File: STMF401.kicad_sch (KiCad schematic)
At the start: 13 parts, among them Y1 X322525MQB4SI

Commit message: feat: firs complete version schemattic
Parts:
- added J6: Conn_01x04_Pin, Connector_PinSocket_2.54mm:PinSocket_1x04_P2.54mm_Vertical, symbol Connector:Conn_01x04_Pin
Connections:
- net +3V3D: now also J6.1 (Pin_1)
- net GND: now also J6.2 (Pin_2)
- net at DD1.46 (PA13): now also J6.3 (Pin_3)
- net at DD1.49 (PA14): now also J6.4 (Pin_4)

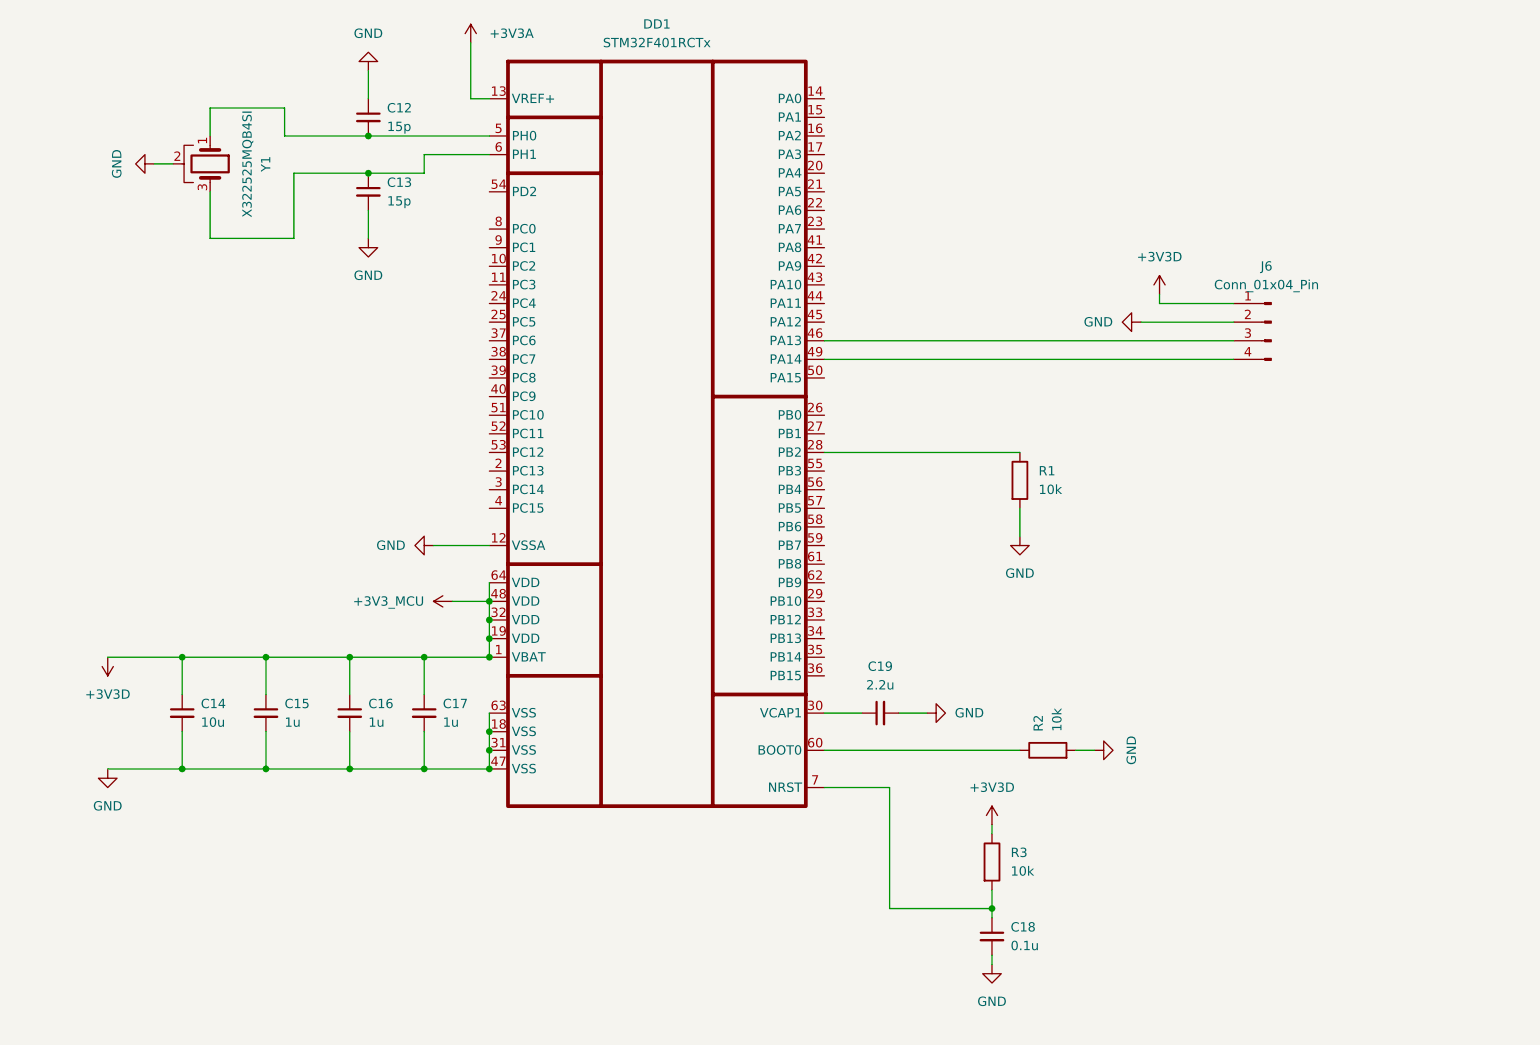
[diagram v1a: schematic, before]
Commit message: feat: Added part of the connections (digital data lines) of the microcontroller
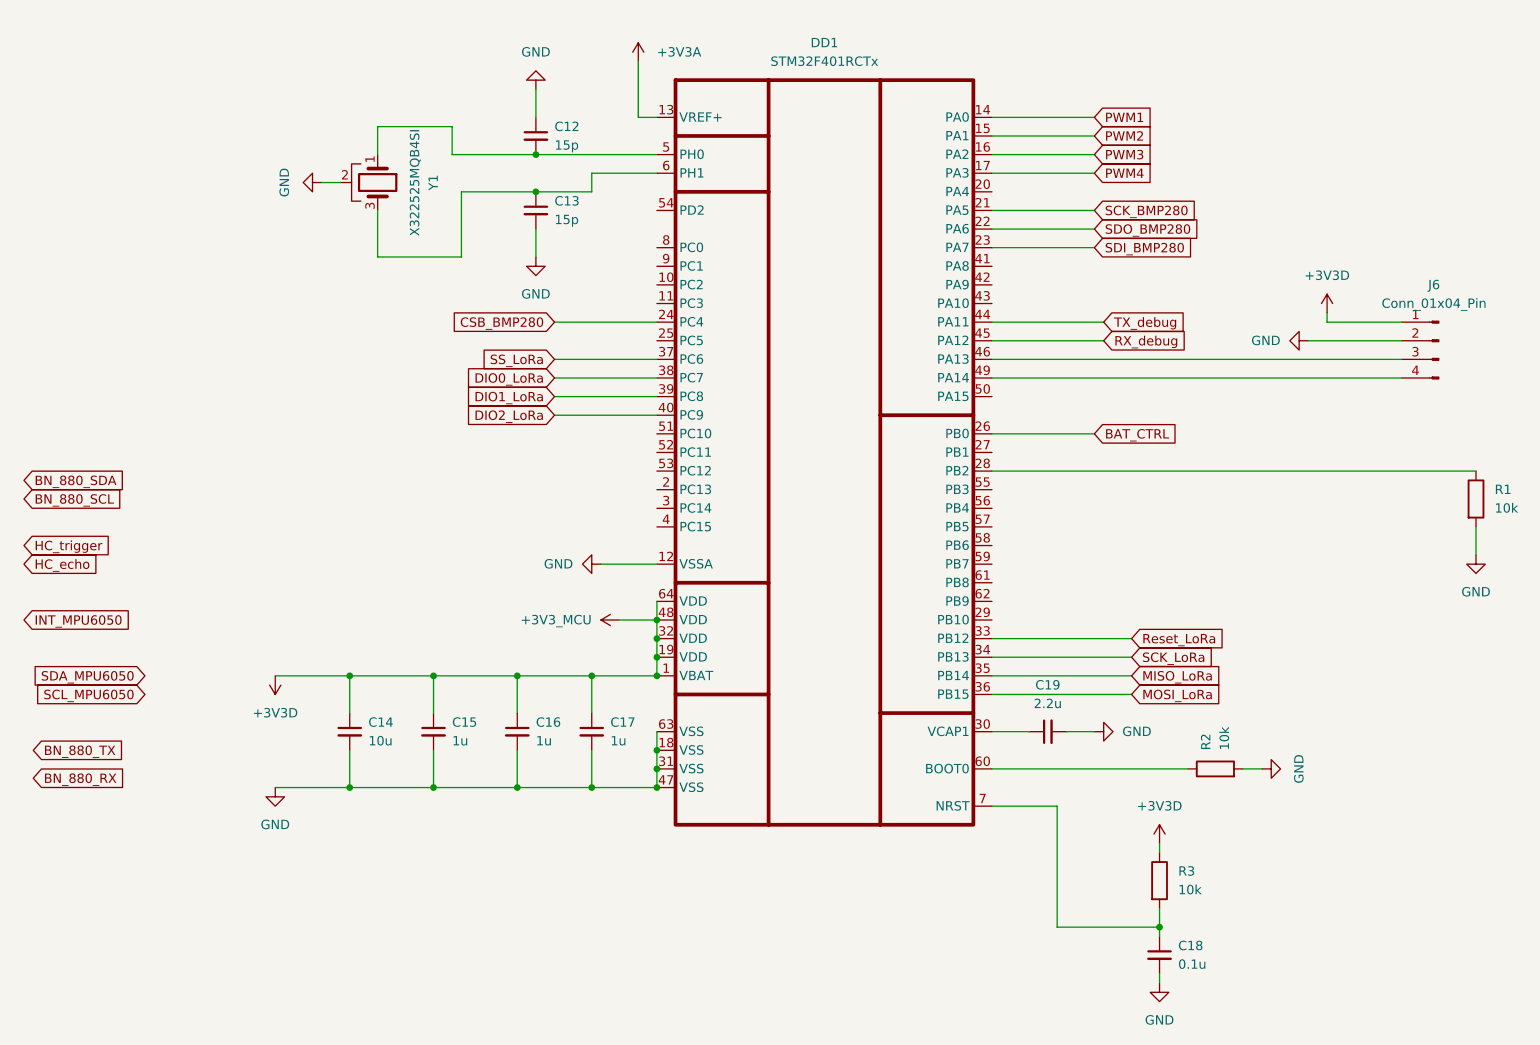
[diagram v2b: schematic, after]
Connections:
- net PWM1: now reaches DD1.14 (PA0)
- net PWM2: now reaches DD1.15 (PA1)
- net PWM3: now reaches DD1.16 (PA2)
- net PWM4: now reaches DD1.17 (PA3)
- net SCK_BMP280: now reaches DD1.21 (PA5)
- net SDO_BMP280: now reaches DD1.22 (PA6)
- net SDI_BMP280: now reaches DD1.23 (PA7)
- net CSB_BMP280: now reaches DD1.24 (PC4)
- net BAT_CTRL: now reaches DD1.26 (PB0)
- net Reset_LoRa: now reaches DD1.33 (PB12)
- net SCK_LoRa: now reaches DD1.34 (PB13)
- net MISO_LoRa: now reaches DD1.35 (PB14)
- net MOSI_LoRa: now reaches DD1.36 (PB15)
- net SS_LoRa: now reaches DD1.37 (PC6)
- net DIO0_LoRa: now reaches DD1.38 (PC7)
- net DIO1_LoRa: now reaches DD1.39 (PC8)
- net DIO2_LoRa: now reaches DD1.40 (PC9)
- net TX_debug: now reaches DD1.44 (PA11)
- net RX_debug: now reaches DD1.45 (PA12)
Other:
- moved on the sheet: C12, C13, C14, C15, C16, C17, C18, C19, DD1, J6, R1, R2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

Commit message: feat: added all connection for MCU
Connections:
- net BN_880_RX: now also DD1.42 (PA9)
- net BN_880_SCL: now also DD1.29 (PB10)
- net BN_880_SDA: now also DD1.55 (PB3)
- net BN_880_TX: now also DD1.43 (PA10)
- net HC_echo: now also DD1.53 (PC12)
- net HC_trigger: now also DD1.52 (PC11)
- net INT_MPU6050: now also DD1.57 (PB5)
- net SCL_MPU6050: now also DD1.58 (PB6)
- net SDA_MPU6050: now also DD1.59 (PB7)
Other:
- moved on the sheet: C12, C13
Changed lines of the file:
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@@
 	(paper "A4")
 	(junction
-		(at 109.22 43.18)
-		(diameter 0)
-		(color 0 0 0 0)
-	)
-	(junction
 		(at 95.25 114.3)
 		(diameter 0)
@@
 	)
 	(junction
+		(at 109.22 43.18)
+		(diameter 0)
+		(color 0 0 0 0)
+	)
+	(junction
 		(at 109.22 48.26)
 		(diameter 0)
@@
 	(wire
 		(pts
+			(xy 109.22 40.64) (xy 109.22 43.18)
+		)
+		(stroke
+			(width 0)
+			(type default)
+		)
+	)
+	(wire
+		(pts
 			(xy 125.73 121.92) (xy 125.73 124.46)
 		)
@@
 	(wire
 		(pts
+			(xy 171.45 63.5) (xy 186.69 63.5)
+		)
+		(stroke
+			(width 0)
+			(type default)
+		)
+	)
+	(wire
+		(pts
 			(xy 82.55 46.99) (xy 80.01 46.99)
 		)
@@
 	(wire
 		(pts
-			(xy 109.22 34.29) (xy 109.22 38.1)
+			(xy 109.22 34.29) (xy 109.22 35.56)
+		)
+		(stroke
+			(width 0)
+			(type default)
+		)
+	)
+	(wire
+		(pts
+			(xy 109.22 50.8) (xy 109.22 48.26)
 		)
 		(stroke
@@
 	(wire
 		(pts
+			(xy 171.45 99.06) (xy 190.5 99.06)
+		)
+		(stroke
+			(width 0)
+			(type default)
+		)
+	)
+	(wire
+		(pts
 			(xy 171.45 50.8) (xy 185.42 50.8)
 		)
@@
 	(wire
 		(pts
+			(xy 171.45 106.68) (xy 190.5 106.68)
+		)
+		(stroke
+			(width 0)
+			(type default)
+		)
+	)
+	(wire
+		(pts
 			(xy 171.45 45.72) (xy 185.42 45.72)
 		)
@@
 	(wire
 		(pts
+			(xy 111.76 83.82) (xy 125.73 83.82)
+		)
+		(stroke
+			(width 0)
+			(type default)
+		)
+	)
+	(wire
+		(pts
 			(xy 73.66 114.3) (xy 83.82 114.3)
 		)
@@
 	(wire
 		(pts
+			(xy 111.76 86.36) (xy 125.73 86.36)
+		)
+		(stroke
+			(width 0)
+			(type default)
+		)
+	)
+	(wire
+		(pts
 			(xy 106.68 129.54) (xy 116.84 129.54)
 		)
@@
 	(wire
 		(pts
+			(xy 171.45 96.52) (xy 190.5 96.52)
+		)
+		(stroke
+			(width 0)
+			(type default)
+		)
+	)
+	(wire
+		(pts
 			(xy 171.45 132.08) (xy 180.34 132.08)
 		)
@@
 	(wire
 		(pts
-			(xy 109.22 53.34) (xy 109.22 57.15)
+			(xy 171.45 60.96) (xy 186.69 60.96)
+		)
+		(stroke
+			(width 0)
+			(type default)
+		)
+	)
+	(wire
+		(pts
+			(xy 109.22 55.88) (xy 109.22 57.15)
 		)
 		(stroke
@@
 	(wire
 		(pts
+			(xy 171.45 88.9) (xy 190.5 88.9)
+		)
+		(stroke
+			(width 0)
+			(type default)
+		)
+	)
+	(wire
+		(pts
 			(xy 116.84 114.3) (xy 125.73 114.3)
 		)
@@
 	(wire
 		(pts
+			(xy 171.45 93.98) (xy 190.5 93.98)
+		)
+		(stroke
+			(width 0)
+			(type default)
+		)
+	)
+	(wire
+		(pts
 			(xy 83.82 114.3) (xy 83.82 119.38)
 		)
@@
 	(global_label "INT_MPU6050"
 		(shape input)
-		(at 39.37 106.68 0)
+		(at 190.5 93.98 0)
 		(fields_autoplaced yes)
 		(effects
@@
 		)
 		(property "Intersheetrefs" "${INTERSHEET_REFS}"
-			(at 55.1156 106.68 0)
+			(at 206.2456 93.98 0)
 			(hide yes)
 			(show_name no)
@@
 	(global_label "BN_880_RX"
 		(shape input)
-		(at 40.64 128.27 0)
+		(at 186.69 60.96 0)
 		(fields_autoplaced yes)
 		(effects
@@
 		)
 		(property "Intersheetrefs" "${INTERSHEET_REFS}"
-			(at 54.2689 128.27 0)
+			(at 200.3189 60.96 0)
 			(hide yes)
 			(show_name no)
@@
 	(global_label "HC_trigger"
 		(shape input)
-		(at 39.37 96.52 0)
+		(at 111.76 83.82 180)
 		(fields_autoplaced yes)
 		(effects
@@
 				(size 1.27 1.27)
 			)
-			(justify left)
+			(justify right)
 		)
 		(property "Intersheetrefs" "${INTERSHEET_REFS}"
-			(at 52.2128 96.52 0)
+			(at 98.9172 83.82 0)
 			(hide yes)
 			(show_name no)
@@
 					(size 1.27 1.27)
 				)
-				(justify left)
+				(justify right)
 			)
 		)
@@
 	(global_label "SCL_MPU6050"
 		(shape input)
-		(at 55.88 116.84 180)
+		(at 190.5 96.52 0)
 		(fields_autoplaced yes)
 		(effects
@@
 				(size 1.27 1.27)
 			)
-			(justify right)
+			(justify left)
 		)
 		(property "Intersheetrefs" "${INTERSHEET_REFS}"
-			(at 39.5297 116.84 0)
+			(at 206.8503 96.52 0)
 			(hide yes)
 			(show_name no)
@@
 					(size 1.27 1.27)
 				)
-				(justify right)
+				(justify left)
 			)
 		)
@@
 	(global_label "BN_880_SCL"
 		(shape input)
-		(at 39.37 90.17 0)
+		(at 190.5 106.68 0)
 		(fields_autoplaced yes)
 		(effects
@@
 		)
 		(property "Intersheetrefs" "${INTERSHEET_REFS}"
-			(at 54.027 90.17 0)
+			(at 205.157 106.68 0)
 			(hide yes)
 			(show_name no)
@@
 	(global_label "BN_880_SDA"
 		(shape input)
-		(at 39.37 87.63 0)
+		(at 190.5 88.9 0)
 		(fields_autoplaced yes)
 		(effects
@@
 		)
 		(property "Intersheetrefs" "${INTERSHEET_REFS}"
-			(at 54.0875 87.63 0)
+			(at 205.2175 88.9 0)
 			(hide yes)
 			(show_name no)
@@
 	(global_label "SDA_MPU6050"
 		(shape input)
-		(at 55.88 114.3 180)
+		(at 190.5 99.06 0)
 		(fields_autoplaced yes)
 		(effects
@@
 				(size 1.27 1.27)
 			)
-			(justify right)
+			(justify left)
 		)
 		(property "Intersheetrefs" "${INTERSHEET_REFS}"
-			(at 39.4692 114.3 0)
+			(at 206.9108 99.06 0)
 			(hide yes)
 			(show_name no)
@@
 					(size 1.27 1.27)
 				)
-				(justify right)
+				(justify left)
 			)
 		)
@@
 	(global_label "HC_echo"
 		(shape input)
-		(at 39.37 99.06 0)
+		(at 111.76 86.36 180)
 		(fields_autoplaced yes)
 		(effects
@@
 				(size 1.27 1.27)
 			)
-			(justify left)
+			(justify right)
 		)
 		(property "Intersheetrefs" "${INTERSHEET_REFS}"
-			(at 50.3985 99.06 0)
+			(at 100.7315 86.36 0)
 			(hide yes)
 			(show_name no)
@@
 					(size 1.27 1.27)
 				)
-				(justify left)
+				(justify right)
 			)
 		)
@@
 	(global_label "BN_880_TX"
 		(shape input)
-		(at 40.64 124.46 0)
+		(at 186.69 63.5 0)
 		(fields_autoplaced yes)
 		(effects
@@
 		)
 		(property "Intersheetrefs" "${INTERSHEET_REFS}"
-			(at 53.9665 124.46 0)
+			(at 200.0165 63.5 0)
 			(hide yes)
 			(show_name no)
@@
 	(symbol
 		(lib_id "Device:C_Small")
-		(at 109.22 40.64 0)
+		(at 109.22 38.1 0)
 		(unit 1)
 		(body_style 1)
@@
 		(fields_autoplaced yes)
 		(property "Reference" "C12"
-			(at 111.76 39.3762 0)
+			(at 111.76 36.8362 0)
 			(show_name no)
 			(do_not_autoplace no)
@@
 		)
 		(property "Value" "15p"
-			(at 111.76 41.9162 0)
+			(at 111.76 39.3762 0)
 			(show_name no)
 			(do_not_autoplace no)
@@
 		)
 		(property "Footprint" "Capacitor_SMD:C_0805_2012Metric_Pad1.18x1.45mm_HandSolder"
-			(at 109.22 40.64 0)
+			(at 109.22 38.1 0)
 			(hide yes)
 			(show_name no)
@@
 		)
 		(property "Datasheet" ""
-			(at 109.22 40.64 0)
+			(at 109.22 38.1 0)
 			(hide yes)
 			(show_name no)
@@
 		)
 		(property "Description" "Unpolarized capacitor, small symbol"
-			(at 109.22 40.64 0)
+			(at 109.22 38.1 0)
 			(hide yes)
 			(show_name no)
@@
 	(symbol
 		(lib_id "Device:C_Small")
-		(at 109.22 50.8 0)
+		(at 109.22 53.34 0)
 		(unit 1)
 		(body_style 1)
@@
 		(fields_autoplaced yes)
 		(property "Reference" "C13"
-			(at 111.76 49.5362 0)
+			(at 111.76 52.0762 0)
 			(show_name no)
 			(do_not_autoplace no)
@@
 		)
 		(property "Value" "15p"
-			(at 111.76 52.0762 0)
+			(at 111.76 54.6162 0)
 			(show_name no)
 			(do_not_autoplace no)
@@
 		)
 		(property "Footprint" "Capacitor_SMD:C_0805_2012Metric_Pad1.18x1.45mm_HandSolder"
-			(at 109.22 50.8 0)
+			(at 109.22 53.34 0)
 			(hide yes)
 			(show_name no)
@@
 		)
 		(property "Datasheet" ""
-			(at 109.22 50.8 0)
+			(at 109.22 53.34 0)
 			(hide yes)
 			(show_name no)
@@
 		)
 		(property "Description" "Unpolarized capacitor, small symbol"
-			(at 109.22 50.8 0)
+			(at 109.22 53.34 0)
 			(hide yes)
 			(show_name no)

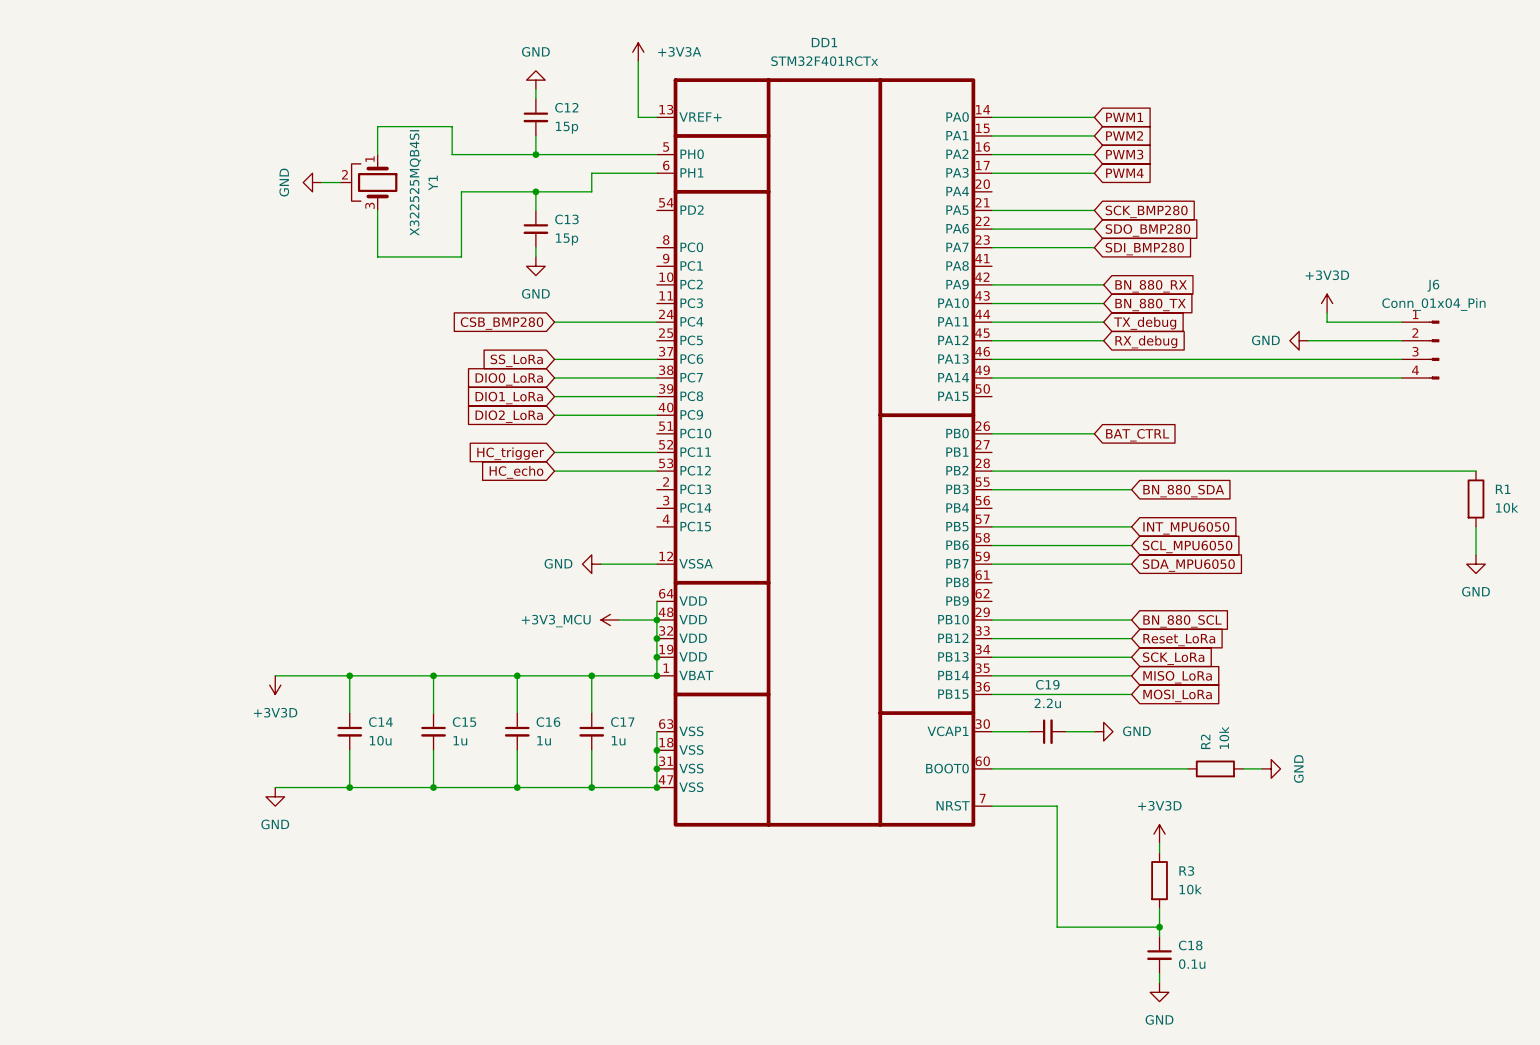
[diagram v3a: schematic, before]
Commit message: feat: complete schematic, and start PCB
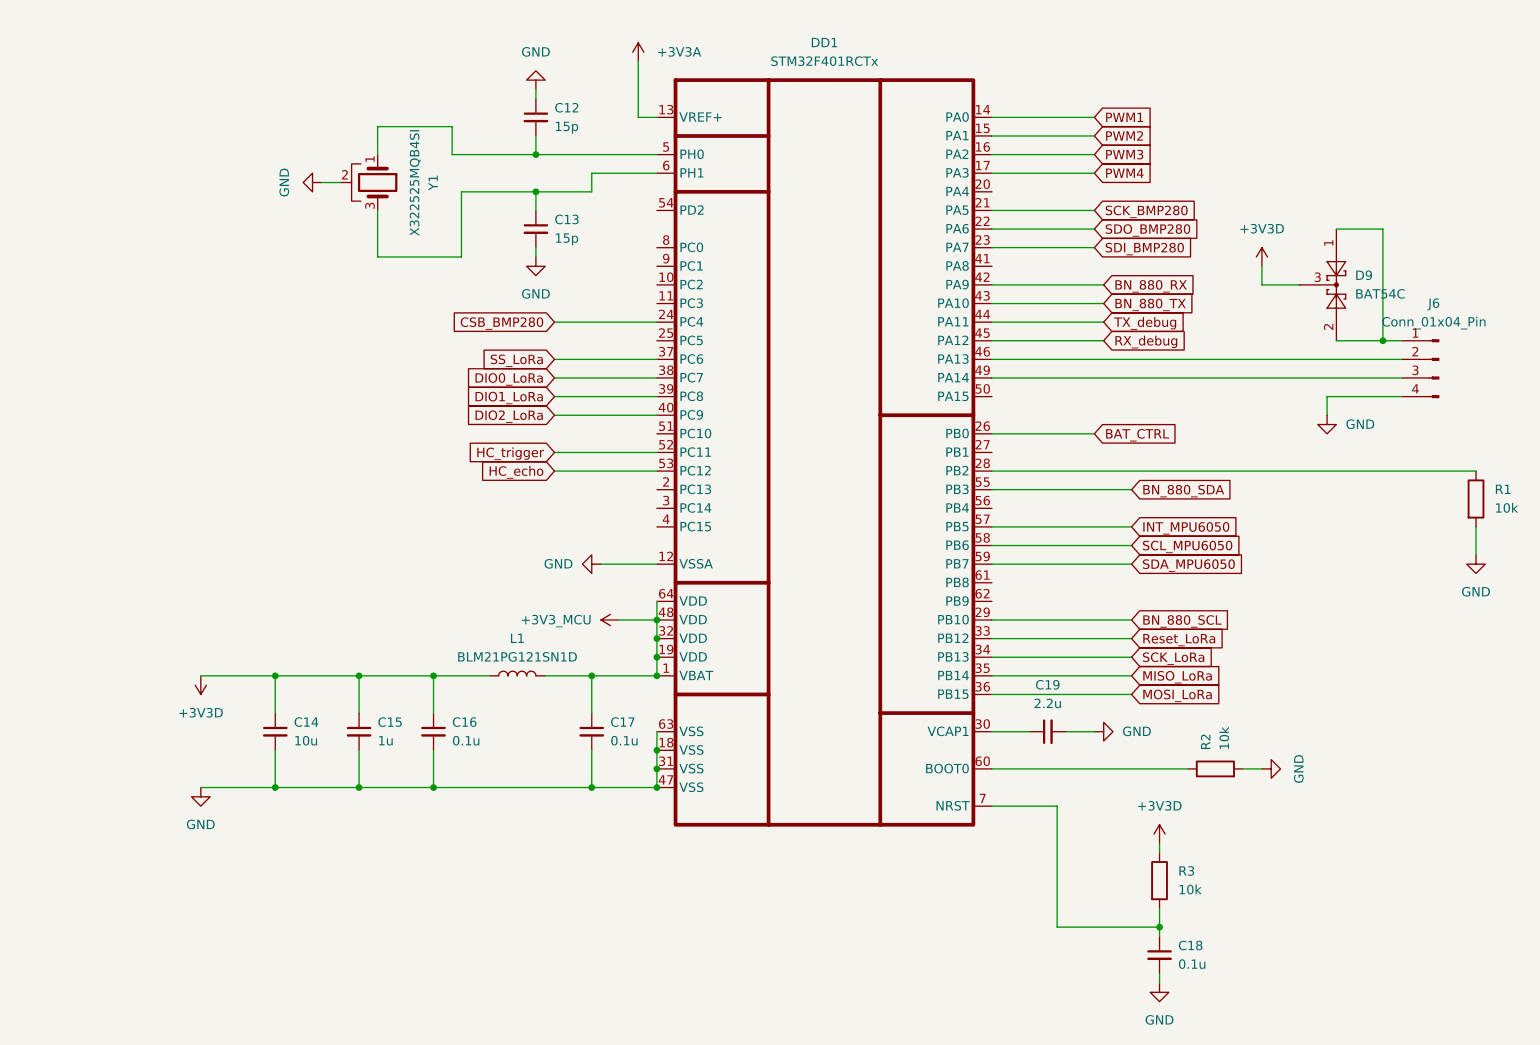
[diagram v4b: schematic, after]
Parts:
- added D9: BAT54C, Package_TO_SOT_SMD:SOT-23_Handsoldering, symbol Diode:BAT54C
- added L1: BLM21PG121SN1D, Inductor_SMD:L_0805_2012Metric_Pad1.05x1.20mm_HandSolder, symbol Inductors:L
- C16, C17: value 1u -> 0.1u
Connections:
- net +3V3D: now also D9.3, L1.1; no longer C17.1, DD1.1 (VBAT), DD1.19 (VDD), DD1.32 (VDD), DD1.48 (VDD), DD1.64 (VDD), J6.1 (Pin_1)
- net GND: now also J6.4 (Pin_4); no longer J6.2 (Pin_2)
- net at DD1.46 (PA13): now also J6.2 (Pin_2); no longer J6.3 (Pin_3)
- net at DD1.49 (PA14): now also J6.3 (Pin_3); no longer J6.4 (Pin_4)
- new net: D9.1, D9.2, J6.1 (Pin_1)
- new net +3V3_MCU: C17.1, DD1.1 (VBAT), DD1.19 (VDD), DD1.32 (VDD), DD1.48 (VDD), DD1.64 (VDD), L1.2
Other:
- moved on the sheet: C14, C15, C16, J6
